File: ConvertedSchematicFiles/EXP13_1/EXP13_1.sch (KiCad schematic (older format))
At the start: 6 parts

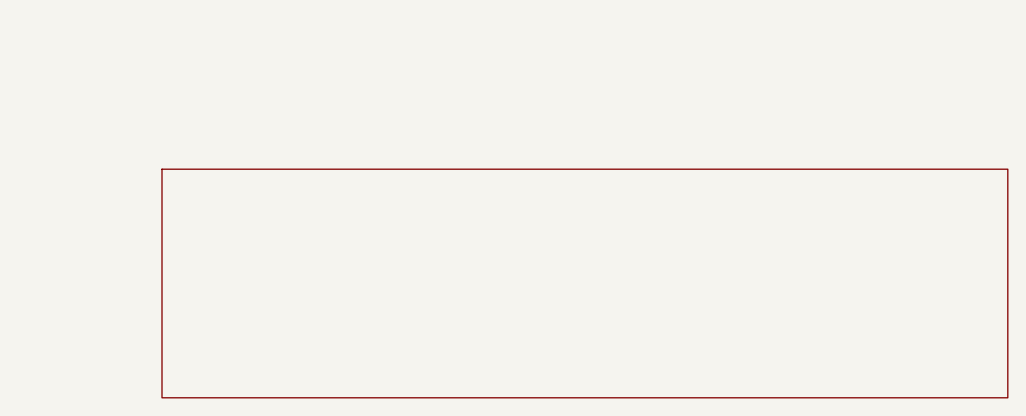
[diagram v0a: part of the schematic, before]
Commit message: Excluded some components. These no longer appear after conversion. When calling shell commands, filenames are in "quotes"
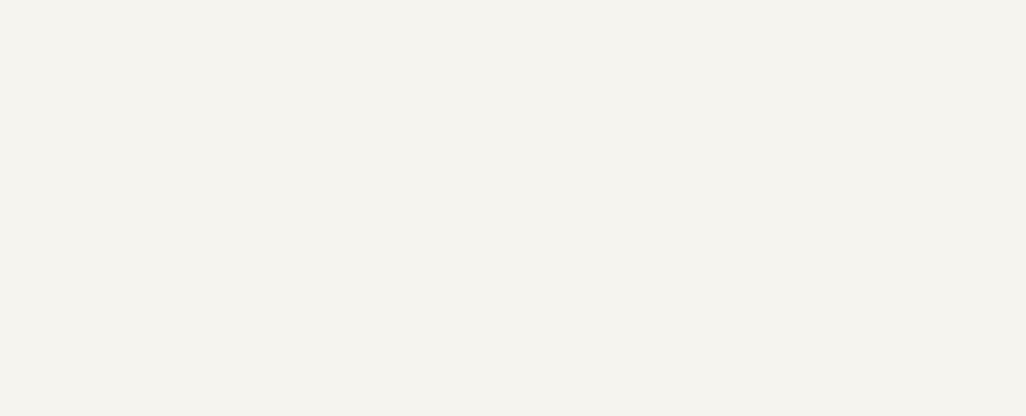
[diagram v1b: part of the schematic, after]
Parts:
- removed titleblk: titleblk, symbol TITLEBLK_PSPICE
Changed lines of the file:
@@
-	1    0    0    1
-$EndComp
-$Comp
-L TITLEBLK_PSPICE titleblk
-U 1 1 74238335
-P 11880 8400
-F 0 "titleblk" H 23760 16800 30  0001 L CNN
-F 1 "titleblk" H 23760 16880 30  0001 L CNN
-	1    11880 8400
 	1    0    0    1
 $EndComp

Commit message: Ports issue fixed. Now annotation for ports is #PWR? function added "itos"
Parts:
- removed EGND: EGND, symbol EGND_PSPICE
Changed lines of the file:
@@
 $EndDescr
 $Comp
-L EGND_PSPICE EGND
+L EGND_PSPICE #PWR1
 U 1 1 14289383
 P 3100 1800
-F 0 "EGND" H 6200 3600 30  0001 L CNN
+F 0 "#PWR1" H 6200 3600 30  0001 L CNN
 F 1 "EGND" H 6200 3680 30  0001 L CNN
 	1    3100 1800

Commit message: Added LICENSE.txt
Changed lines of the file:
@@
 $EndDescr
 $Comp
-L EGND_PSPICE #PWR1
+L GND #PWR1
 U 1 1 14289383
 P 3100 1800

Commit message: Orientation fix. Library components are now inverted, with +ve y axis going up. In Schematic files, +ve y axis is downwards. This is how the KiCad libraries are. As a result of the above fixed, the converted GND is now oriented correctly.
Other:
- moved on the sheet: I1, TX1
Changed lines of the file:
@@
 F 1 "EGND" H 6200 3680 30  0001 L CNN
 	1    3100 1800
-	1    0    0    1
+	1    0    0    -1
 $EndComp
 $Comp
@@
 F 1 "R" H 3100 1380 30  0000 L CNN
 	1    3100 1300
-	0    -1    1    0
+	0    1    1    0
 $EndComp
 $Comp
@@
 F 1 "1MEG" H 2300 2090 30  0000 L CNN
 	1    2300 2000
-	1    0    0    1
+	1    0    0    -1
 $EndComp
 $Comp
@@
 F 1 "IPWL" H 1400 1380 30  0000 L CNN
 	1    1400 1300
-	1    0    0    1
+	1    0    0    -1
 $EndComp
 $Comp
@@
 F 1 "XFRM_LINEAR" H 2200 1280 30  0000 L CNN
 	1    2200 1200
-	1    0    0    1
+	1    0    0    -1
 $EndComp
 Wire Wire Line

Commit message: Removed the use of exec, wrote basename function, made integration with eSim easier.
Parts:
- added titleblk: titleblk, symbol titleblk_PSPICE
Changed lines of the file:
@@
-EESchema Schematic File Version 2  date Sunday 27 February 2000 11:34:45 AM IST
+EESchema Schematic File Version 2  date
 LIBS:power
 LIBS:device
@@
 LIBS:contrib
 LIBS:valves
-LIBS:ConvertedSchematicFiles/EXP13_1-cache
 EELAYER 25  0
 EELAYER END
@@
 Sheet 1 1
 Title ""
-Date "27 Feb 2000"
+Date ""
 Rev ""
 Comp ""
@@
 	1    0    0    -1
 $EndComp
+$Comp
+L titleblk_PSPICE titleblk
+U 1 1 74238335
+P 11880 8400
+F 0 "titleblk" H 23760 16800 30  0001 L CNN
+F 1 "titleblk" H 23760 16880 30  0001 L CNN
+	1    11880 8400
+	1    0    0    -1
+$EndComp
